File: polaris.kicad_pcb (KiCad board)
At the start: 4 copper layers, 75 x 155 mm, 163 parts, among them J101 XT60-M, J102 SPI, J103 I2C, J104 PB, J105 SWD, J106 PYRO0, J107 PYRO1, J108 PYRO2, J109 PYRO3, J110 PYRO4, J111 PYRO5, J112 SERVO0, J113 SERVO1, J114 SERVO2, J115 SERVO3, J116 SERVO4, J117 SERVO5, J118 RADIO, J119 POWER, J301 USB_C_Receptacle_USB2.0_16P, J401 GNSS, J501 XT60-M, Q201 IRLZ44N, Q202 IRLZ44N, Q401 Q_NMOS, Q501 IRLZ44N, Q502 IRLZ44N, Q503 IRLZ44N, Q504 IRLZ44N, Q505 IRLZ44N, Q506 IRLZ44N, SW401 SW_Push, SW402 SW_Push, U1101 THD-2528-11SD-GF, U1201 W25Q128JVS, U201 BQ24005, U202 LM74700, U203 LM74700, U204 LMR51430, U205 LMR51430, U301 USBLC6-2SC6, U302 CH224K, U303 USBLC6-2SC6, U401 STM32F446VETx, U501 PC817, U502 PC817, U503 CD4051B, U504 PC817, U505 PC817, U506 PC817, U507 PC817, U601 ICM-42688-P, U701 LSM6DSO32TR, U801 MS5607, U901 LPS22HH, Y401 YXC YSX321SL

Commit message: Added more power (3.3V) headers for more powering peripherals
Continued laying out tracks
Revised order of connections to pyrochannel mux for easier routing
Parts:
- removed J401: GNSS, Connector_JST:JST_XH_B4B-XH-A_1x04_P2.50mm_Vertical
- added J120: GNSS, Connector_JST:JST_XH_B4B-XH-A_1x04_P2.50mm_Vertical, F.Cu at (95.5, 27.9)
- added J121: POWER, TerminalBlock:TerminalBlock_Xinya_XY308-2.54-2P_1x02_P2.54mm_Horizontal, F.Cu at (57.0, 69.6)
- added J122: POWER, TerminalBlock:TerminalBlock_Xinya_XY308-2.54-2P_1x02_P2.54mm_Horizontal, F.Cu at (64.7, 69.6)
- added R403: 100k, Resistor_SMD:R_0603_1608Metric, F.Cu at (158.2, 83.5)
- added R410: 22k1, Resistor_SMD:R_0603_1608Metric, F.Cu at (158.2, 86.0)
- C207, C208, C209: value 4u7 -> 10u; footprint Capacitor_SMD:C_0603_1608Metric -> Capacitor_SMD:C_0805_2012Metric
- C215: value 22u -> 100n; footprint Capacitor_SMD:C_0805_2012Metric -> Capacitor_SMD:C_0603_1608Metric
- C408: footprint Capacitor_SMD:C_0603_1608Metric -> Capacitor_SMD:C_0805_2012Metric
- R404, R405, R408, R409: moved to F.Cu
- moved R204 141.0 mm to (148.0, 117.5)
- moved R205 141.0 mm to (148.0, 120.0)
- moved C201 137.2 mm to (140.0, 111.3), turned to -90 degrees
- moved D201 135.9 mm to (144.0, 117.5), turned to 180 degrees
- moved D202 135.8 mm to (144.0, 120.0), turned to 180 degrees
- moved C202 135.1 mm to (141.5, 108.0), turned to 90 degrees
- moved R202 113.7 mm to (127.5, 109.0), turned to -90 degrees
- moved R201 112.9 mm to (126.5, 106.5)
- moved R203 101.2 mm to (128.5, 101.0), turned to -90 degrees
- moved R901 86.0 mm to (127.5, 82.0), turned to 90 degrees
- moved R520 82.3 mm to (97.5, 102.0), turned to -90 degrees
- moved R902 80.5 mm to (123.5, 80.7), turned to 90 degrees
- moved R506 80.1 mm to (93.5, 114.5), turned to 90 degrees
- moved R513 77.8 mm to (95.0, 114.5), turned to 90 degrees
- moved R505 77.7 mm to (92.0, 114.5), turned to 90 degrees
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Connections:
- C201 pad 1: /1_Power/BATT_APG -> Net-(U201-CR)
- C202 pad 1: Net-(U201-TMR_SEL) -> Net-(U201-CR)
- C202 pad 2: GND -> Net-(U201-TMR_SEL)
- J105 pad 1: +3.3V -> GND
- J105 pad 4: GND -> +3.3V
- J118 pad 1: +3.3V -> GND
- J118 pad 2: /3_NavigationProcessor/RF_TX -> /3_NavigationProcessor/RF_RX
- J118 pad 3: /3_NavigationProcessor/RF_RX -> /3_NavigationProcessor/RF_TX
- J118 pad 4: GND -> +3.3V
- U201 pad 12: /1_Power/BATT_APG -> Net-(U201-CR)
- U401 pad 23: /3_NavigationProcessor/GPS_RX -> /3_NavigationProcessor/GNSS_RX
- U401 pad 24: /3_NavigationProcessor/GPS_TX -> /3_NavigationProcessor/GNSS_TX
- U401 pad 77: unconnected-(U401-PA15-Pad77) -> /3_NavigationProcessor/VBUS_DETECT
- U503 pad 1: /4_Pyrochannels/PYRO_C4 -> /4_Pyrochannels/PYRO_C5
- U503 pad 12: /4_Pyrochannels/PYRO_C3 -> /4_Pyrochannels/PYRO_C0
- U503 pad 13: /4_Pyrochannels/PYRO_C2 -> /4_Pyrochannels/PYRO_C1
- U503 pad 14: /4_Pyrochannels/PYRO_C1 -> /4_Pyrochannels/PYRO_C2
- U503 pad 15: /4_Pyrochannels/PYRO_C0 -> /4_Pyrochannels/PYRO_C3
- U503 pad 5: /4_Pyrochannels/PYRO_C5 -> /4_Pyrochannels/PYRO_C4
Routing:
- net /4_Pyrochannels/PYRO_5: track 0.00 -> 85.9 mm
- net /3_NavigationProcessor/I2C2_SCL: track 0.00 -> 72.2 mm, vias 0 -> 4
- net /4_Pyrochannels/PYRO_4: track 0.00 -> 70.2 mm
- net GND: track 19.1 -> 80.6 mm, vias 5 -> 13
- net /3_NavigationProcessor/GNSS_TX: track 0.00 -> 49.2 mm, vias 0 -> 2
- net /4_Pyrochannels/PYRO_3: track 0.00 -> 47.0 mm
- net Net-(U401-NRST): track 0.00 -> 46.9 mm, vias 0 -> 2
- net /3_NavigationProcessor/GNSS_RX: track 0.00 -> 46.4 mm, vias 0 -> 2
- net /3_NavigationProcessor/RF_RX: track 0.00 -> 45.9 mm, vias 0 -> 3
- net /3_NavigationProcessor/RF_TX: track 0.00 -> 45.6 mm, vias 0 -> 3
- net Net-(U401-BOOT0): track 0.00 -> 44.3 mm, vias 0 -> 2
- net /3_NavigationProcessor/PB3: track 0.00 -> 39.3 mm, vias 0 -> 1
- net /4_Pyrochannels/PYRO_2: track 0.00 -> 39.2 mm
- net /3_NavigationProcessor/PB4: track 0.00 -> 37.2 mm, vias 0 -> 1
- net /3_NavigationProcessor/PB5: track 0.00 -> 35.0 mm, vias 0 -> 1
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- added copper zone on B.Cu, net +5V
- added copper zone on F.Cu, net /1_Power/USB_VCC
- added copper zone on F.Cu, net GND
- added copper zone on B.Cu, net POWER
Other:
- board text added: "Done"
- board text removed: "VREF"

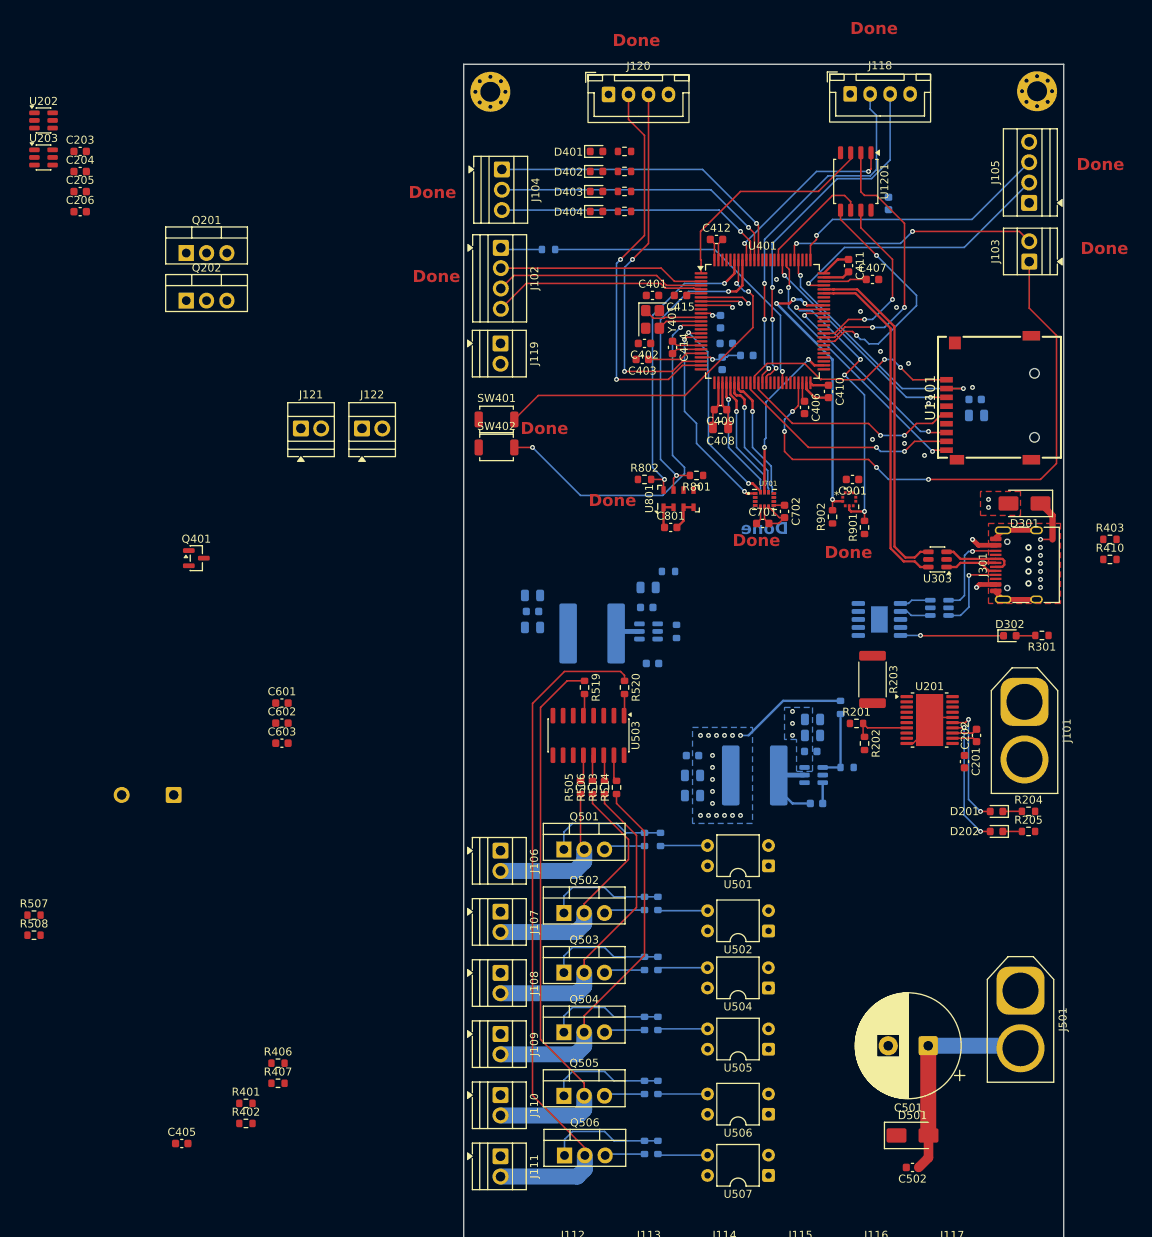
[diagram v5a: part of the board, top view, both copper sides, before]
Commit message: Continued routing traces
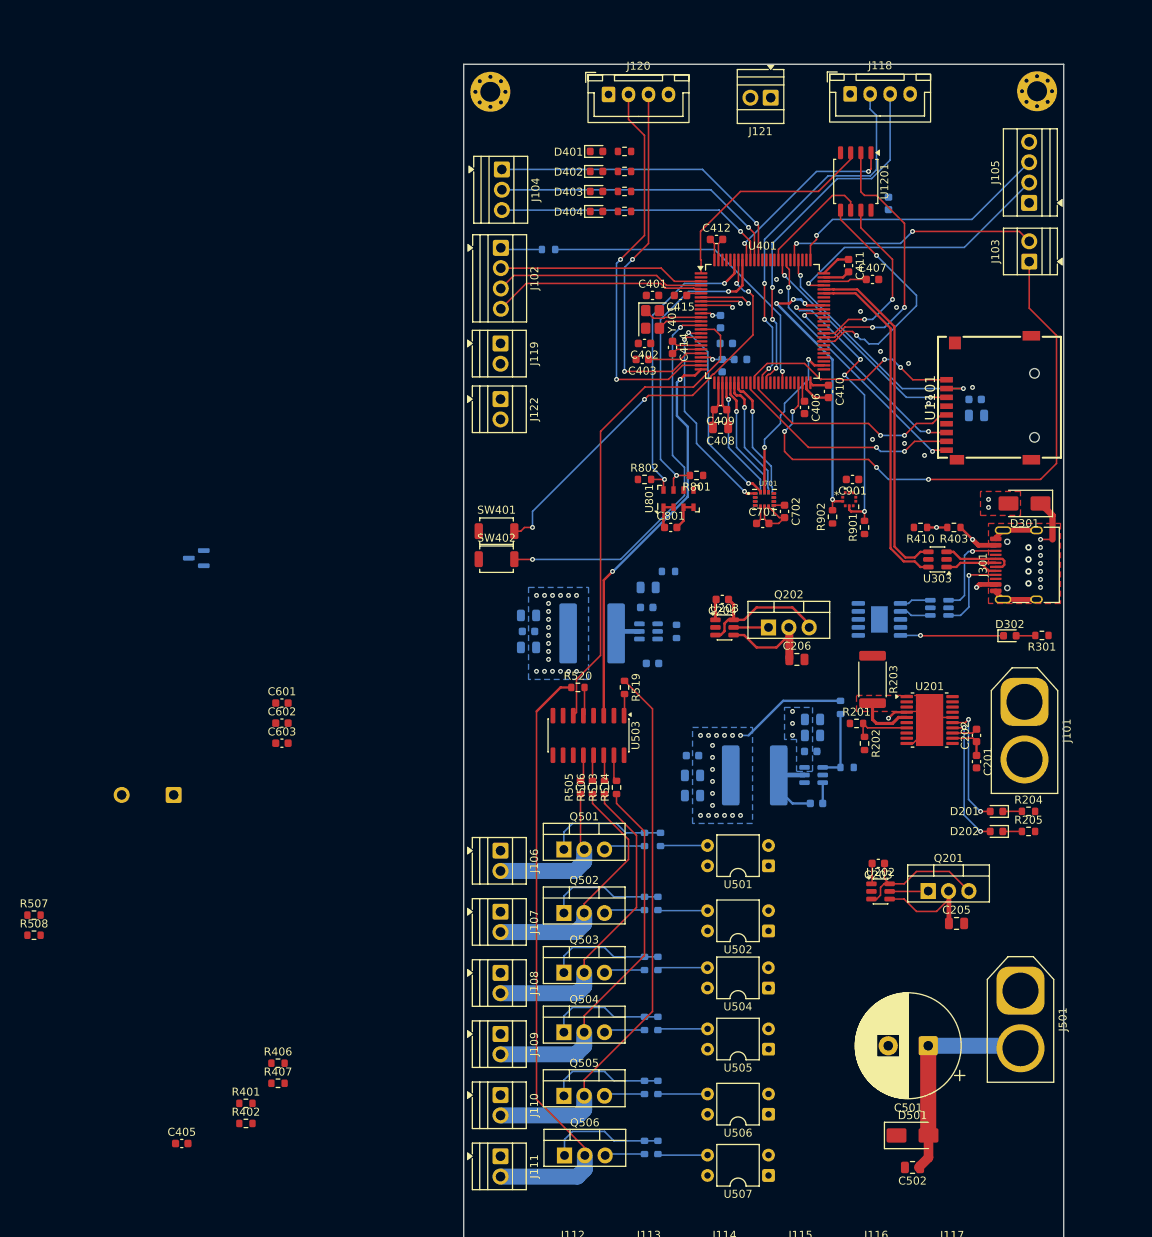
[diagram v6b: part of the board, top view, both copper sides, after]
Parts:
- C205, C206, C502: footprint Capacitor_SMD:C_0603_1608Metric -> Capacitor_SMD:C_0805_2012Metric
- Q401: moved to B.Cu
- moved C205 142.7 mm to (139.0, 131.5)
- moved U202 142.2 mm to (129.5, 127.5)
- moved C203 133.7 mm to (129.2, 124.0), turned to 180 degrees
- moved Q201 122.3 mm to (135.5, 127.5)
- moved C206 105.6 mm to (119.0, 98.5)
- moved U203 103.4 mm to (110.0, 94.5)
- moved C204 96.5 mm to (109.7, 91.0), turned to 180 degrees
- moved Q202 83.5 mm to (115.5, 94.5)
- moved J121 71.8 mm to (115.8, 28.3), turned to 180 degrees
- moved R410 24.0 mm to (134.5, 82.0), turned to 180 degrees
- moved R403 19.6 mm to (138.7, 82.0), turned to 180 degrees
- moved J122 17.7 mm to (82.0, 66.0), turned to -90 degrees
- moved SW401 14.0 mm to (81.5, 82.5)
- moved SW402 14.0 mm to (81.5, 86.0)
- moved R520 5.83 mm to (91.7, 102.0), turned to 0 degrees
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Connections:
- U503 pad 1: /4_Pyrochannels/PYRO_C5 -> /4_Pyrochannels/PYRO_C4
- U503 pad 5: /4_Pyrochannels/PYRO_C4 -> /4_Pyrochannels/PYRO_C5
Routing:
- net /3_NavigationProcessor/~{MUX_EN}: track 0.00 -> 61.5 mm
- net /3_NavigationProcessor/PYRO_SENSE: track 0.00 -> 50.3 mm, vias 0 -> 2
- net POWER: track 0.07 -> 27.0 mm
- net /1_Power/USB_VCC: track 12.4 -> 34.9 mm, vias 13 -> 14
- net VBAT_VIN: track 0.00 -> 18.0 mm
- net /4_Pyrochannels/PYRO_5: track 85.9 -> 76.2 mm
- net Net-(U401-BOOT0): track 44.3 -> 51.8 mm, vias 2 -> 4
- net /1_Power/IN: track 0.00 -> 6.83 mm
- net Net-(Q201-G): track 0.00 -> 4.84 mm
- net Net-(Q202-G): track 0.00 -> 4.36 mm
- net Net-(U203-VCAP): track 0.00 -> 2.59 mm
- net Net-(U202-VCAP): track 0.00 -> 2.59 mm
- net /3_NavigationProcessor/VBUS_DETECT: track 0.00 -> 2.53 mm, vias 0 -> 1
- net Net-(U401-NRST): track 46.9 -> 49.3 mm
- net Net-(U201-CR): track 3.18 -> 4.90 mm
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- added copper zone on B.Cu, net +3.3V
- added copper zone on F.Cu, net /1_Power/IN
